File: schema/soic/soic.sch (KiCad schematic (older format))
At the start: 5 parts, among them J1 Conn_01x04_Male, J2 Conn_01x04_Male, U1 LF398_SOIC8

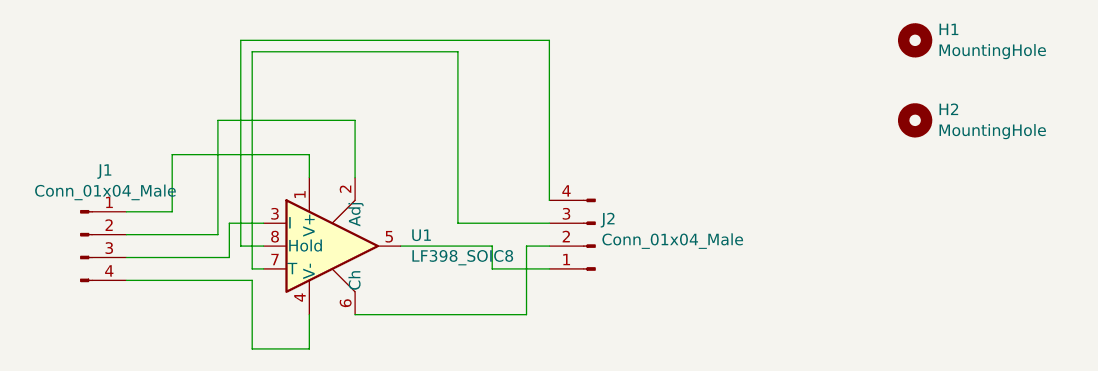
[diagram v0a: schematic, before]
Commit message: installation instruction, 1/2 sided PCB instructions
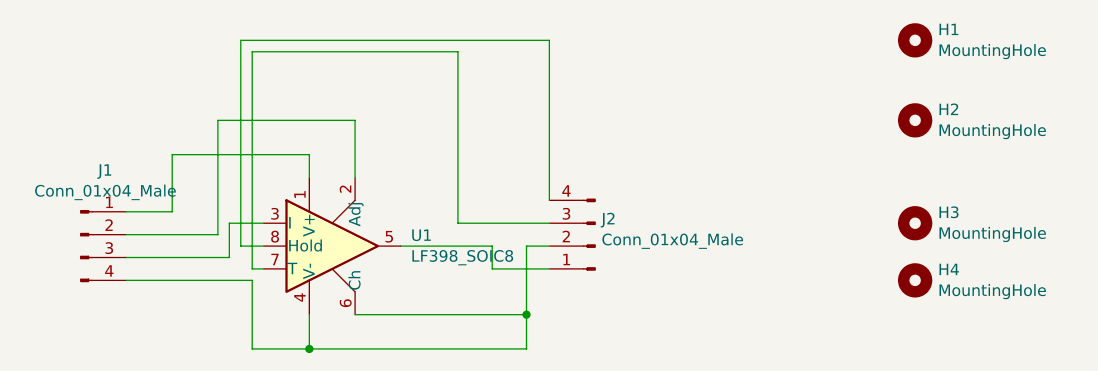
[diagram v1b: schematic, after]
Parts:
- added H3, H4: MountingHole, MountingHole:MountingHole_2.1mm, symbol Mechanical:MountingHole
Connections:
- net at J1.4 (Pin_4), U1.4 (V-): now also J2.2 (Pin_2), U1.6 (Ch)
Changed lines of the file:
@@
+	1    0    0    -1
+$EndComp
+Wire Wire Line
+	4250 2650 5200 2650
+Wire Wire Line
+	5200 2650 5200 2500
+Connection ~ 4250 2650
+Connection ~ 5200 2500
+$Comp
+L Mechanical:MountingHole H3
+U 1 1 6225ED9F
+P 6900 2100
+F 0 "H3" H 7000 2146 50  0000 L CNN
+F 1 "MountingHole" H 7000 2055 50  0000 L CNN
+F 2 "MountingHole:MountingHole_2.1mm" H 6900 2100 50  0001 C CNN
+F 3 "~" H 6900 2100 50  0001 C CNN
+	1    6900 2100
+	1    0    0    -1
+$EndComp
+$Comp
+L Mechanical:MountingHole H4
+U 1 1 6225EF9E
+P 6900 2350
+F 0 "H4" H 7000 2396 50  0000 L CNN
+F 1 "MountingHole" H 7000 2305 50  0000 L CNN
+F 2 "MountingHole:MountingHole_2.1mm" H 6900 2350 50  0001 C CNN
+F 3 "~" H 6900 2350 50  0001 C CNN
+	1    6900 2350
 	1    0    0    -1
 $EndComp

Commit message: ardrill command, pad2pad&soic projects
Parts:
- removed H3, H4: MountingHole, MountingHole:MountingHole_2.1mm, symbol Mechanical:MountingHole
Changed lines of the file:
@@
 Connection ~ 4250 2650
 Connection ~ 5200 2500
-$Comp
-L Mechanical:MountingHole H3
-U 1 1 6225ED9F
-P 6900 2100
-F 0 "H3" H 7000 2146 50  0000 L CNN
-F 1 "MountingHole" H 7000 2055 50  0000 L CNN
-F 2 "MountingHole:MountingHole_2.1mm" H 6900 2100 50  0001 C CNN
-F 3 "~" H 6900 2100 50  0001 C CNN
-	1    6900 2100
-	1    0    0    -1
-$EndComp
-$Comp
-L Mechanical:MountingHole H4
-U 1 1 6225EF9E
-P 6900 2350
-F 0 "H4" H 7000 2396 50  0000 L CNN
-F 1 "MountingHole" H 7000 2305 50  0000 L CNN
-F 2 "MountingHole:MountingHole_2.1mm" H 6900 2350 50  0001 C CNN
-F 3 "~" H 6900 2350 50  0001 C CNN
-	1    6900 2350
-	1    0    0    -1
-$EndComp
 $EndSCHEMATC
